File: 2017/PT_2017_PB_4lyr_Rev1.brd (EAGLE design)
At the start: 162.5 x 209.5 mm, 158 parts, among them Q12 2N7002

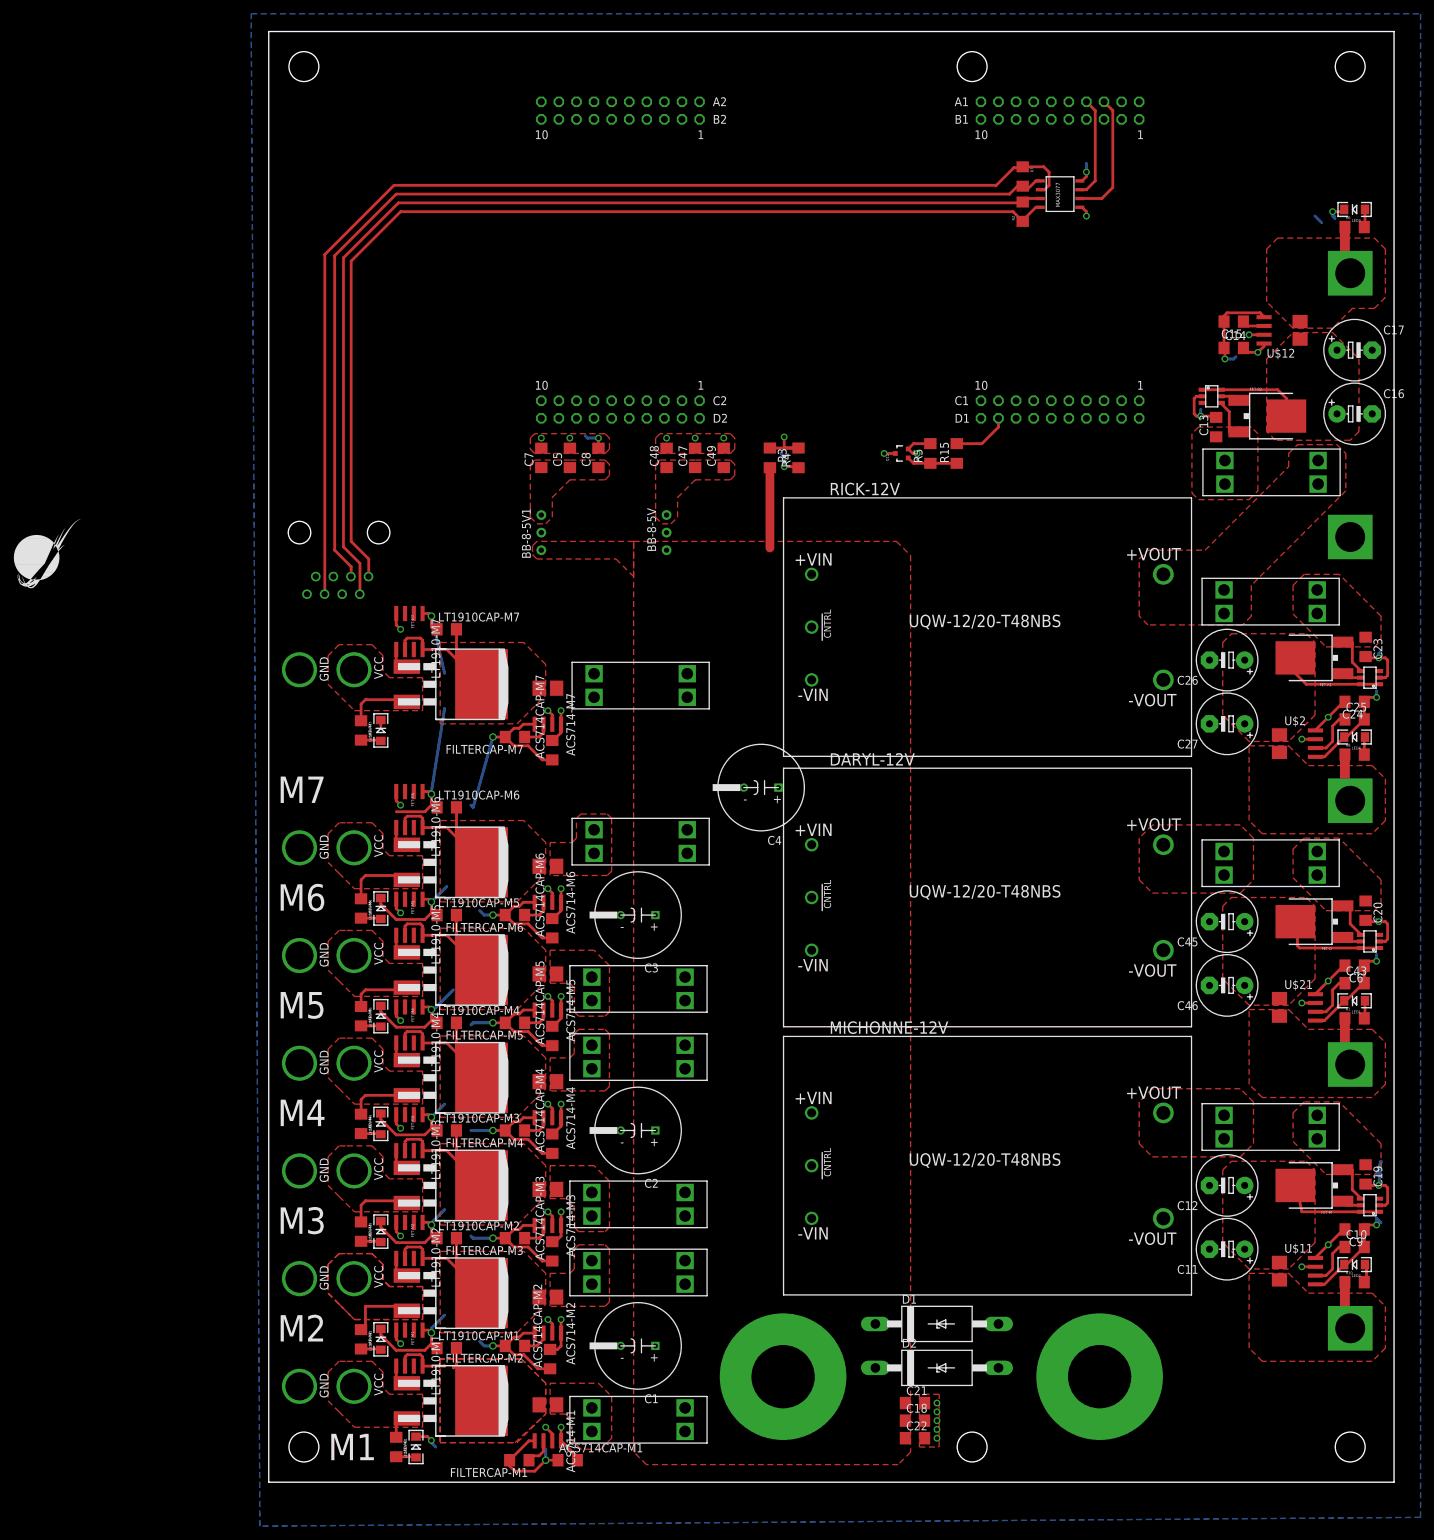
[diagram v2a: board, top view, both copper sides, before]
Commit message: Spaced Out Motor Busses
Components for motor busses are more spread out and more solderable.
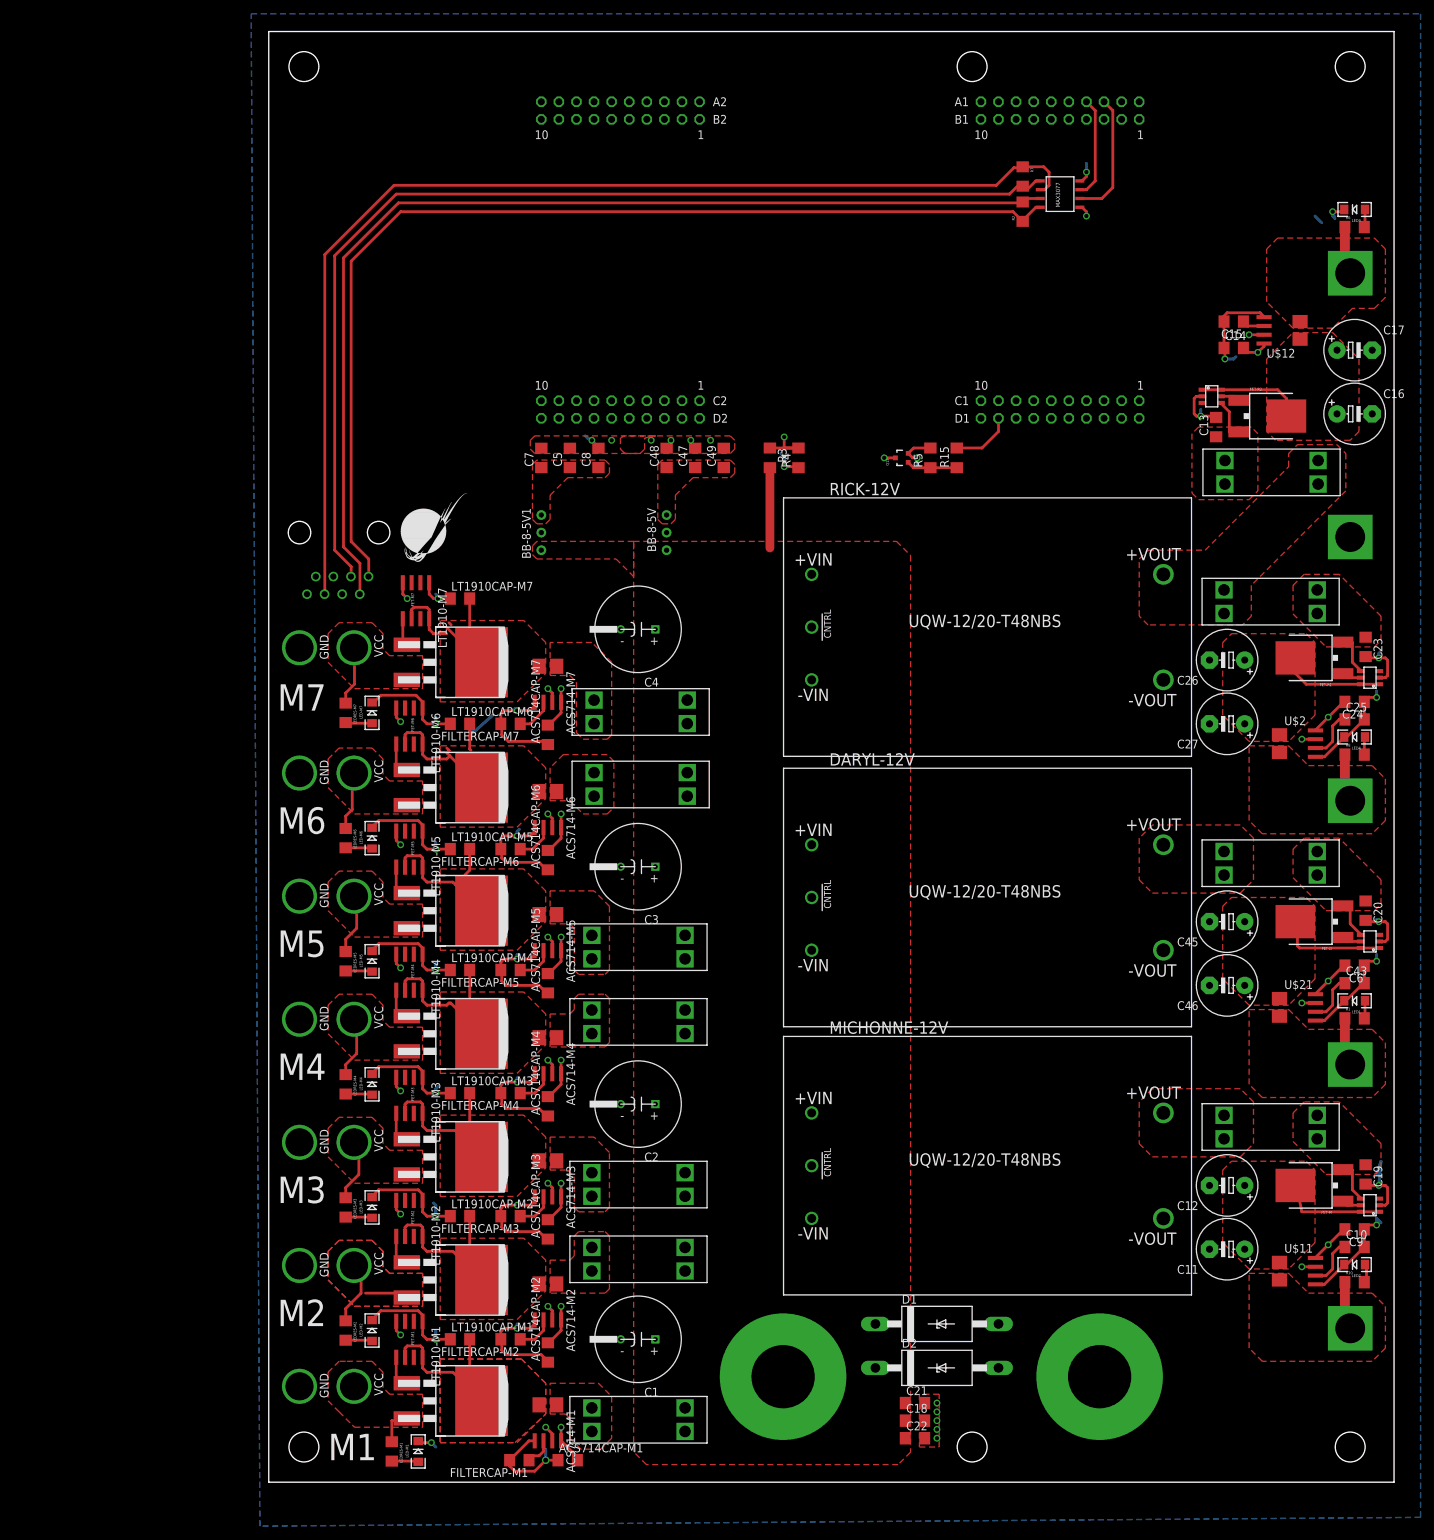
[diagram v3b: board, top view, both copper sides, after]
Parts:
- moved U$41 56.0 mm to (19.1, 132.1)
- moved C4 29.0 mm to (53.3, 123.2)
- moved LT1910CAP-M6 12.2 mm to (27.6, 109.5)
- moved LT1910-M6 12.1 mm to (20.3, 109.2)
- moved ACS714-M6 10.8 mm to (40.3, 97.2)
- moved FET-M6 10.8 mm to (24.1, 105.4)
- moved U$20 10.8 mm to (1.27, 106.4)
- moved LEDRES-M6 10.4 mm to (11.1, 93.0)
- moved LED-M6 10.2 mm to (14.9, 93.0)
- moved ACS714CAP-M6 9.86 mm to (40.3, 89.9)
- moved LT1910-M5 9.84 mm to (20.3, 91.4)
- moved LT1910CAP-M5 9.71 mm to (27.6, 91.4)
- moved FILTERCAP-M6 9.55 mm to (34.9, 91.4)
- moved ACS714-M5 8.57 mm to (40.3, 79.4)
- moved FET-M5 8.57 mm to (24.1, 87.6)
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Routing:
- net 3.3V: track 138.7 -> 173.4 mm
- net GND: track 372.5 -> 344.0 mm
- net SIG-M7: track 65.8 -> 42.9 mm
- net SIG-M6: track 77.0 -> 62.7 mm
- net DRAIN-M1: track 12.0 -> 24.7 mm
- net IMEAS-M6: track 138.3 -> 127.5 mm
- net SIG-M5: track 92.7 -> 81.9 mm
- net IMEAS-M5: track 153.0 -> 144.5 mm
- net SIG-M4: track 105.7 -> 97.1 mm
- net IMEAS-M4: track 171.4 -> 165.0 mm
- net SIG-M3: track 124.8 -> 118.5 mm
- net SOURCE-M2: track 11.0 -> 15.9 mm
- net DRAIN-M4: track 20.4 -> 25.2 mm
- net DRAIN-M2: track 20.4 -> 25.0 mm
- net DRAIN-M3: track 20.4 -> 25.0 mm
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- added copper zone on layer 1, net V_BATT_M7

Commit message: Spaced Out 12V Busses
Components easier to solder and fuses are easier to reach.
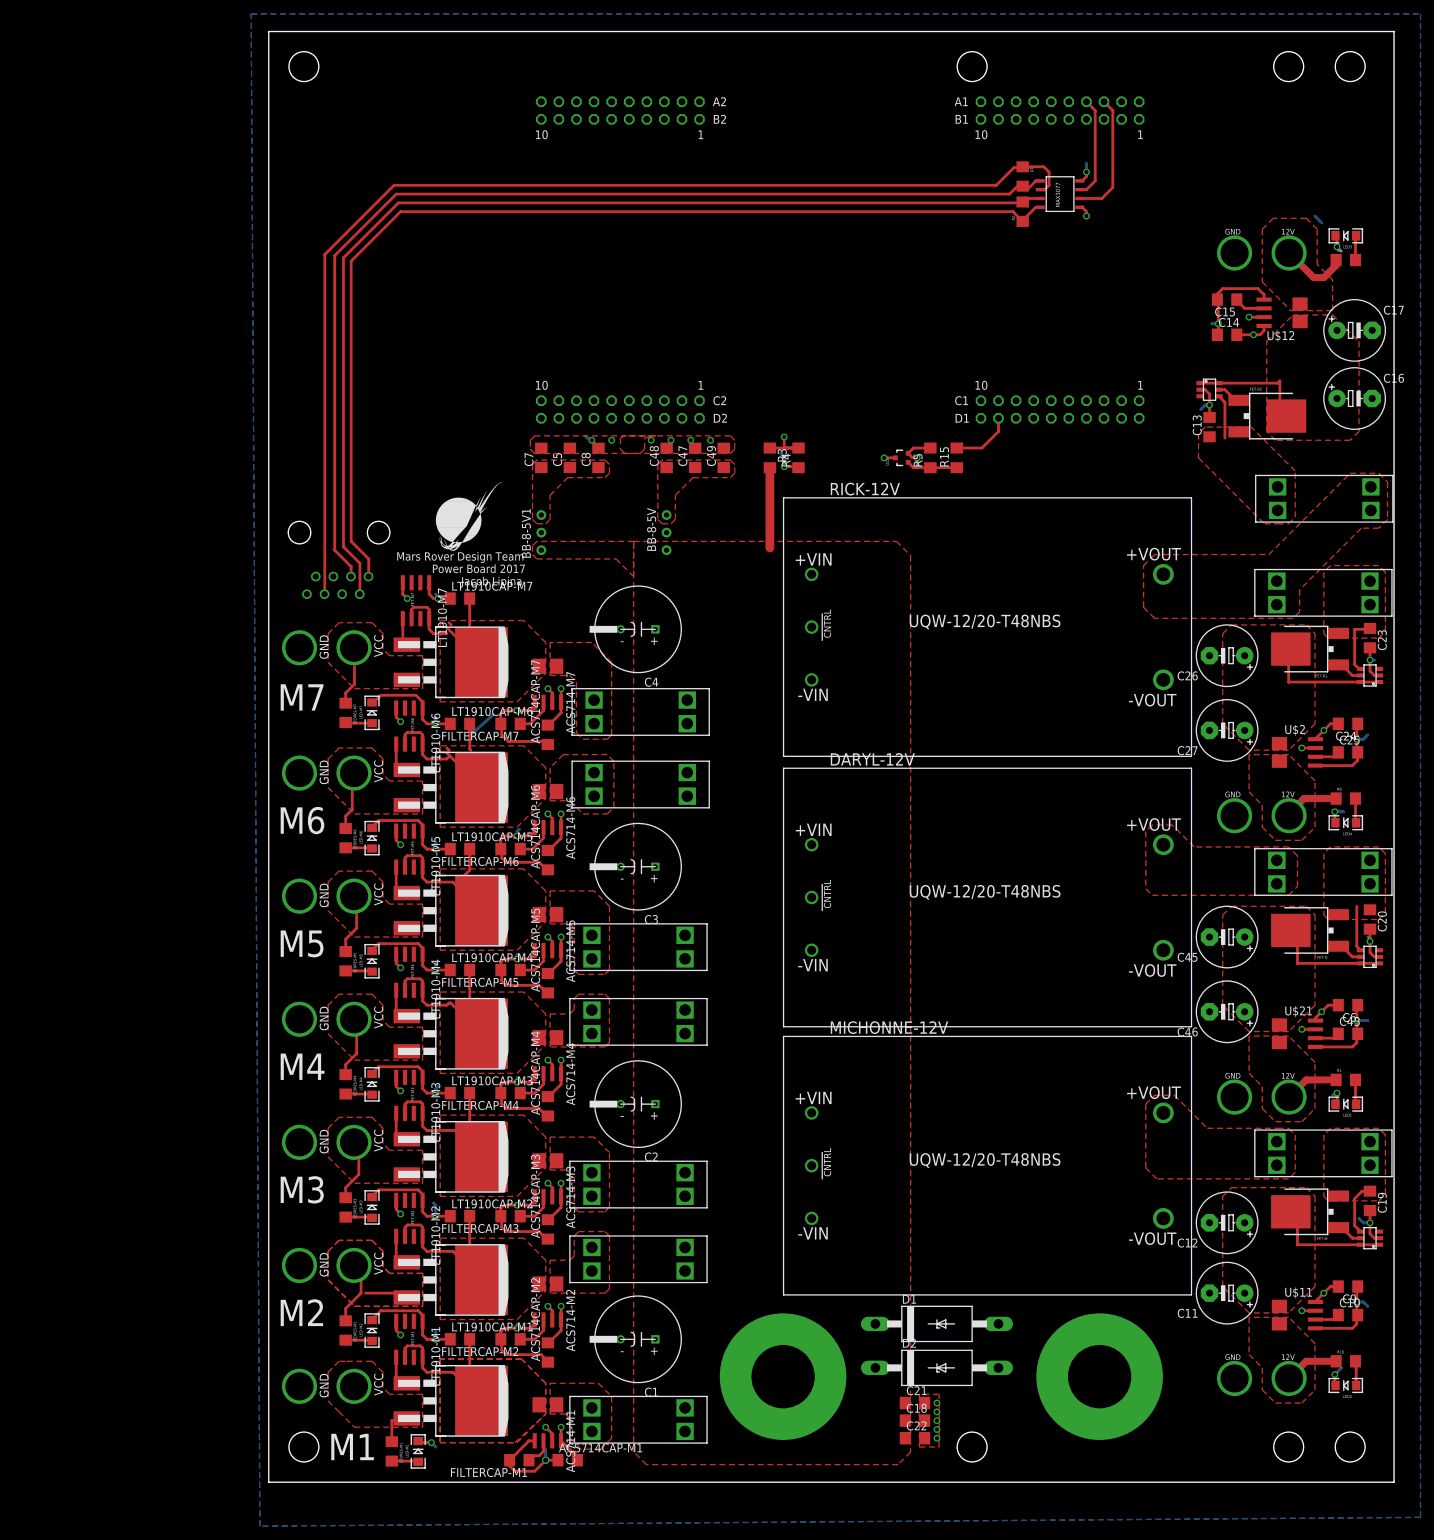
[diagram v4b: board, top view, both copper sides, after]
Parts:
- removed U$17, U$18, U$25, U$33: BUS_BAR_MOUNTING_HOLE, MRDT-Connectors:1/8IN_BUS_BAR
- added J1, J2, J3, J4: APP_2POS_CONFIG12V_VERT, MRDT-Connectors:APP45_12V_VERT_CONFIG
- added U$5: MOUNTING_HOLE#8, MRDT-Hardware:#8_SCREW
- U$14, U$26, U$27, U$28, U$29, U$30, U$31, U$32, U$36, U$37, U$38: device MRDT-Hardware:3557-2 -> MRDT-Hardware:BLOCK_3557-2
- U$16: value BUS_BAR_MOUNTING_HOLE -> MOUNTING_HOLE#8; device MRDT-Connectors:1/8IN_BUS_BAR -> MRDT-Hardware:#8_SCREW
- moved U$16 31.1 mm to (147.3, 204.5)
- moved LED2 17.5 mm to (155.6, 14.0)
- moved LED1 15.0 mm to (155.6, 54.6)
- moved LED4 12.4 mm to (155.6, 95.2)
- moved R10 11.5 mm to (155.6, 17.5)
- moved C10 9.89 mm to (155.9, 24.1)
- moved R1 8.98 mm to (155.6, 58.1)
- moved U$14 8.52 mm to (162.2, 44.1)
- moved U$31 8.52 mm to (142.6, 145.4)
- moved C9 8.31 mm to (155.9, 28.3)
- moved U$30 7.73 mm to (162.2, 84.8)
- moved U$32 7.73 mm to (162.2, 125.1)
- moved C43 7.36 mm to (155.9, 64.8)
- moved R8 6.48 mm to (155.6, 98.7)
- moved C11 6.35 mm to (138.4, 27.3)
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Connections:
- net ARM-12V-SIG renamed EXTRA-12V-SIG
- removed net 12V-AUX-ARM: R10.1, U$11.4, U$18.P$2
- new net 12V-AUX-EXTRA: J4.VCC, R10.1, U$11.4
- net 12V-AUX-ACT: now also J3.VCC; no longer U$17.P$2
- net 12V-AUX-COM: now also J1.VCC; no longer U$33.P$2
- net 12V-AUX-LOGIC: now also J2.VCC; no longer U$16.P$2
- net GND: now also J1.GND, J2.GND, J3.GND, J4.GND; no longer U$25.P$2
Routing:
- net 3.3V: track 173.4 -> 123.9 mm
- net GND: track 344.0 -> 335.5 mm, vias 38 -> 41
- net 12V-AUX-EXTRA: track 0.00 -> 7.82 mm
- net 12V-AUX-ARM: track 6.98 -> 0.00 mm
- net EXTRA-12V-SIG: track 193.9 -> 200.2 mm
- net ACT-12V-SIG: track 154.7 -> 158.5 mm
- net N$4: track 7.27 -> 3.64 mm
- net N$10: track 7.27 -> 3.64 mm
- net N$12: track 7.27 -> 3.83 mm
- net N$22: track 15.0 -> 18.0 mm
- net 12V-AUX-LOGIC: track 6.98 -> 9.76 mm
- net LOGIC-12V-SIG: track 48.7 -> 46.1 mm
- net N$9: track 6.00 -> 8.49 mm
- net N$19: track 15.2 -> 17.1 mm
- net N$2: track 6.00 -> 7.80 mm
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- added copper zone on layer 1, net 12V-AUX-EXTRA
- removed copper zone on layer 1, net 12V-AUX-ARM
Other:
- board text added: "Mars Rover Design Team Power Board 2017 Jacob Lipina"
